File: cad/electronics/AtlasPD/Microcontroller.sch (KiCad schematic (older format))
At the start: 1 part, among them U2 NUCLEO-L432KC

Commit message: Started adding ROS stuff to Arduino, Started Laying out Electrical Diagram
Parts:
- removed U2: NUCLEO-L432KC, NUCLEO-L432KC:MODULE_NUCLEO-L432KC, symbol NUCLEO-L432KC:NUCLEO-L432KC
- added A?: Arduino_UNO_R3, Module:Arduino_UNO_R3, symbol MCU_Module:Arduino_UNO_R3
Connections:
- net labels added: +5V, GND
- wire segments 0 -> 7
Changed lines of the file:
@@
 $Descr A4 11693 8268
 encoding utf-8
-Sheet 3 3
+Sheet 3 4
 Title ""
 Date ""
@@
 $EndDescr
 $Comp
-L NUCLEO-L432KC:NUCLEO-L432KC U2
-U 1 1 60A304B8
-P 2100 2500
-F 0 "U2" H 2100 3477 50  0000 C CNN
-F 1 "NUCLEO-L432KC" H 2100 3386 50  0000 C CNN
-F 2 "NUCLEO-L432KC:MODULE_NUCLEO-L432KC" H 2100 2500 50  0001 L BNN
-F 3 "" H 2100 2500 50  0001 L BNN
-F 4 "N/A" H 2100 2500 50  0001 L BNN "PARTREV"
-F 5 "Manufacturer Recommendations" H 2100 2500 50  0001 L BNN "STANDARD"
-F 6 "N/A" H 2100 2500 50  0001 L BNN "MAXIMUM_PACKAGE_HEIGHT"
-F 7 "ST Microelectronics" H 2100 2500 50  0001 L BNN "MANUFACTURER"
-	1    2100 2500
+L MCU_Module:Arduino_UNO_R3 A?
+U 1 1 61273F77
+P 3750 2050
+F 0 "A?" H 3250 3100 50  0000 C CNN
+F 1 "Arduino_UNO_R3" H 3250 3000 50  0000 C CNN
+F 2 "Module:Arduino_UNO_R3" H 3750 2050 50  0001 C CIN
+F 3 "https://www.arduino.cc/en/Main/arduinoBoardUno" H 3750 2050 50  0001 C CNN
+	1    3750 2050
 	1    0    0    -1
 $EndComp
 $Comp
-L NUCLEO-L432KC:NUCLEO-L432KC U2
-U 2 1 60A30D6D
-P 4500 2600
-F 0 "U2" H 4500 3577 50  0000 C CNN
-F 1 "NUCLEO-L432KC" H 4500 3486 50  0000 C CNN
-F 2 "NUCLEO-L432KC:MODULE_NUCLEO-L432KC" H 4500 2600 50  0001 L BNN
-F 3 "" H 4500 2600 50  0001 L BNN
-F 4 "N/A" H 4500 2600 50  0001 L BNN "PARTREV"
-F 5 "Manufacturer Recommendations" H 4500 2600 50  0001 L BNN "STANDARD"
-F 6 "N/A" H 4500 2600 50  0001 L BNN "MAXIMUM_PACKAGE_HEIGHT"
-F 7 "ST Microelectronics" H 4500 2600 50  0001 L BNN "MANUFACTURER"
-	2    4500 2600
+L power:+5V #PWR?
+U 1 1 61275645
+P 3950 850
+F 0 "#PWR?" H 3950 700 50  0001 C CNN
+F 1 "+5V" H 3965 1023 50  0000 C CNN
+F 2 "" H 3950 850 50  0001 C CNN
+F 3 "" H 3950 850 50  0001 C CNN
+	1    3950 850
 	1    0    0    -1
 $EndComp
+$Comp
+L power:GND #PWR?
+U 1 1 61275C13
+P 3750 3350
+F 0 "#PWR?" H 3750 3100 50  0001 C CNN
+F 1 "GND" H 3755 3177 50  0000 C CNN
+F 2 "" H 3750 3350 50  0001 C CNN
+F 3 "" H 3750 3350 50  0001 C CNN
+	1    3750 3350
+	1    0    0    -1
+$EndComp
+Wire Wire Line
+	3650 3150 3650 3250
+Wire Wire Line
+	3650 3250 3750 3250
+Wire Wire Line
+	3750 3250 3750 3150
+Wire Wire Line
+	3750 3250 3850 3250
+Wire Wire Line
+	3850 3250 3850 3150
+Connection ~ 3750 3250
+Wire Wire Line
+	3750 3250 3750 3350
+Wire Wire Line
+	3950 850  3950 1050
 $EndSCHEMATC

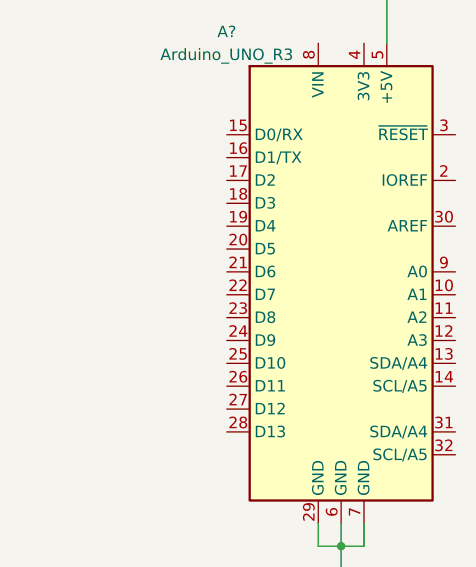
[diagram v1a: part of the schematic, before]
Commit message: Added LDO
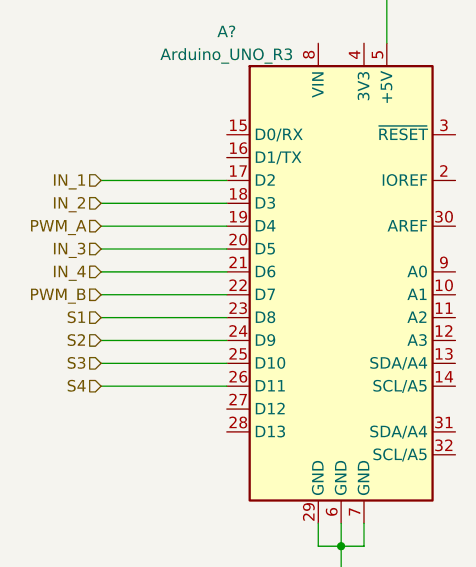
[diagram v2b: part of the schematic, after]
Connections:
- net IN_1: now reaches A?.17 (D2)
- net IN_2: now reaches A?.18 (D3)
- net PWM_A: now reaches A?.19 (D4)
- net IN_3: now reaches A?.20 (D5)
- net IN_4: now reaches A?.21 (D6)
- net PWM_B: now reaches A?.22 (D7)
- net S1: now reaches A?.23 (D8)
- net S2: now reaches A?.24 (D9)
- net S3: now reaches A?.25 (D10)
- net S4: now reaches A?.26 (D11)
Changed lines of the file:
@@
 Wire Wire Line
 	3950 850  3950 1050
+Text HLabel 2700 1650 0    50   Input ~ 0
+IN_1
+Text HLabel 2700 1750 0    50   Input ~ 0
+IN_2
+Text HLabel 2700 1850 0    50   Input ~ 0
+PWM_A
+Text HLabel 2700 1950 0    50   Input ~ 0
+IN_3
+Text HLabel 2700 2050 0    50   Input ~ 0
+IN_4
+Text HLabel 2700 2150 0    50   Input ~ 0
+PWM_B
+Text HLabel 2700 2250 0    50   Input ~ 0
+S1
+Text HLabel 2700 2350 0    50   Input ~ 0
+S2
+Text HLabel 2700 2450 0    50   Input ~ 0
+S3
+Text HLabel 2700 2550 0    50   Input ~ 0
+S4
+Wire Wire Line
+	2700 1650 3250 1650
+Wire Wire Line
+	2700 1750 3250 1750
+Wire Wire Line
+	2700 1850 3250 1850
+Wire Wire Line
+	2700 1950 3250 1950
+Wire Wire Line
+	2700 2050 3250 2050
+Wire Wire Line
+	2700 2150 3250 2150
+Wire Wire Line
+	2700 2250 3250 2250
+Wire Wire Line
+	2700 2350 3250 2350
+Wire Wire Line
+	2700 2450 3250 2450
+Wire Wire Line
+	2700 2550 3250 2550
 $EndSCHEMATC

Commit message: Added part annotations
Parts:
- gave numbers to parts that had none: 1
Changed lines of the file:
@@
 $EndDescr
 $Comp
-L MCU_Module:Arduino_UNO_R3 A?
+L MCU_Module:Arduino_UNO_R3 A1
 U 1 1 61273F77
 P 3750 2050
-F 0 "A?" H 3250 3100 50  0000 C CNN
+F 0 "A1" H 3250 3100 50  0000 C CNN
 F 1 "Arduino_UNO_R3" H 3250 3000 50  0000 C CNN
 F 2 "Module:Arduino_UNO_R3" H 3750 2050 50  0001 C CIN
@@
 $EndComp
 $Comp
-L power:+5V #PWR?
+L power:+5V #PWR04
 U 1 1 61275645
 P 3950 850
-F 0 "#PWR?" H 3950 700 50  0001 C CNN
+F 0 "#PWR04" H 3950 700 50  0001 C CNN
 F 1 "+5V" H 3965 1023 50  0000 C CNN
 F 2 "" H 3950 850 50  0001 C CNN
@@
 $EndComp
 $Comp
-L power:GND #PWR?
+L power:GND #PWR03
 U 1 1 61275C13
 P 3750 3350
-F 0 "#PWR?" H 3750 3100 50  0001 C CNN
+F 0 "#PWR03" H 3750 3100 50  0001 C CNN
 F 1 "GND" H 3755 3177 50  0000 C CNN
 F 2 "" H 3750 3350 50  0001 C CNN
